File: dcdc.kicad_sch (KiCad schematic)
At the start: 198 parts, among them U11 SIC431AED-T1-GE3, U12 SIC431AED-T1-GE3, U13 SIC431AED-T1-GE3, U22 INA219AIDCNR, U50 INA219AIDCNR, U60 INA219AIDCNR, U65 SIC431AED-T1-GE3, U66 INA219AIDCNR, U69 TPS564247DRLR, U7 TPS564247DRLR, U75 SIC431AED-T1-GE3, U76 INA219AIDCNR, U8 SIC431AED-T1-GE3

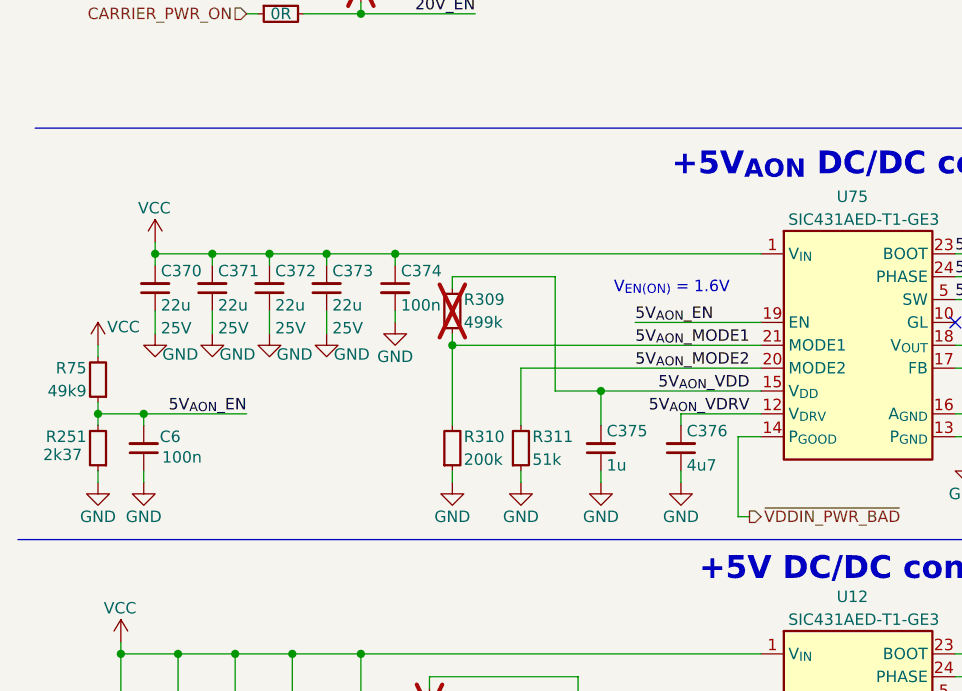
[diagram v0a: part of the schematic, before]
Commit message: Fix R251 symbol on schematic, improve readability of U75 EN voltage divider
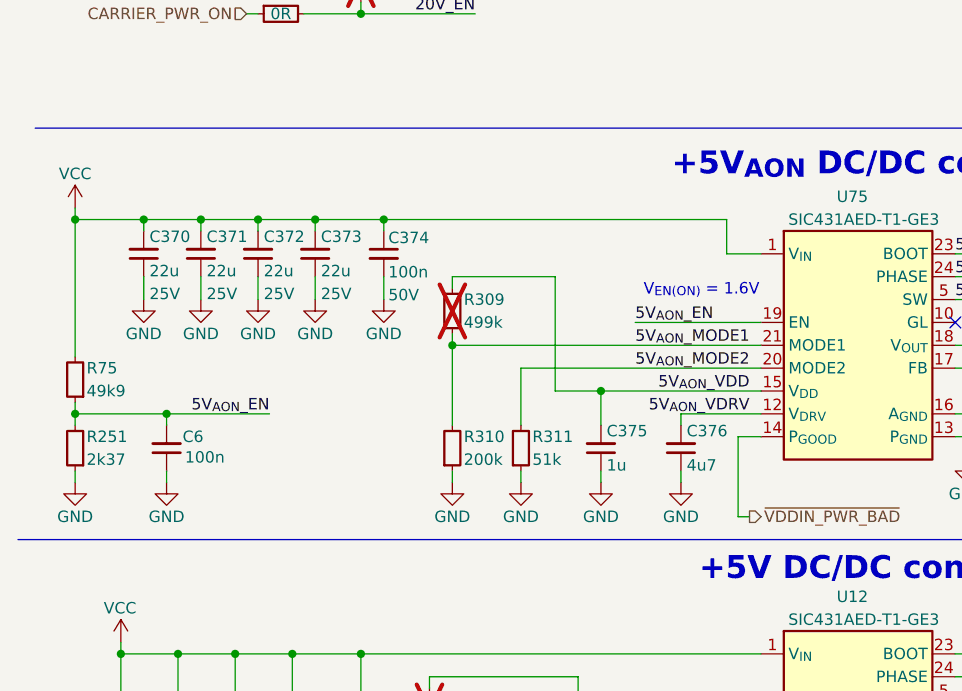
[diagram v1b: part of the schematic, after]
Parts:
- R251: value R_499k_0402 -> R_2k37_0402
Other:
- moved on the sheet: C370, C371, C372, C373, C374, C6, R251, R75

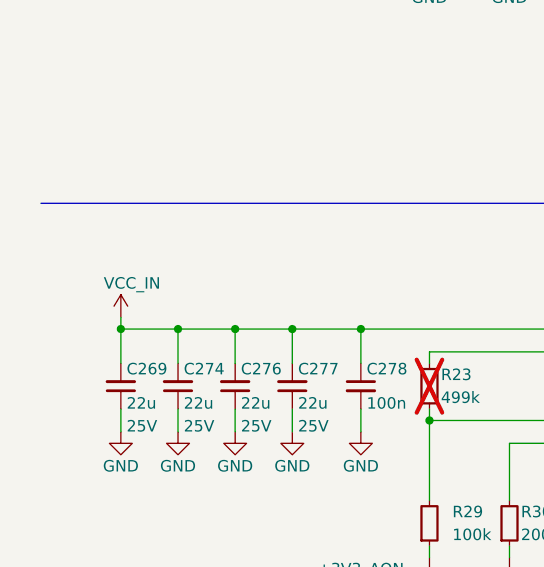
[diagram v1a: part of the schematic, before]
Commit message: Fix +20V converter now is power up from Vcc not Vcc_in
After this change +20V DC/DC converter is safe from reverse voltage
connected to board
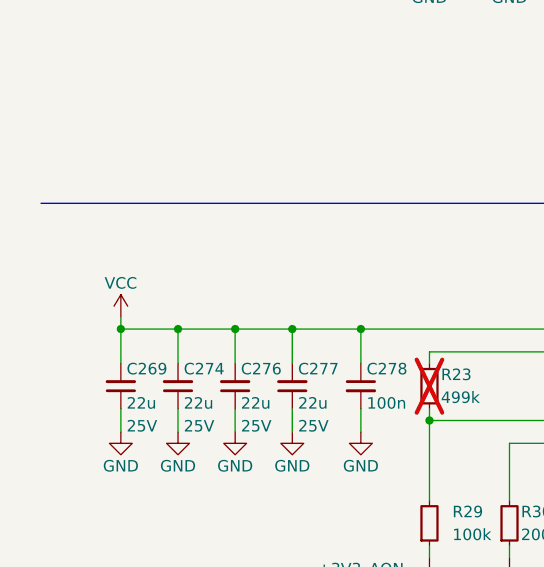
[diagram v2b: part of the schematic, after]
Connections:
- net VCC_IN is gone; now on net VCC: C269.2, C274.2, C276.2, C277.2, C278.1, U65.1 (V_{IN}), U65.2 (V_{IN}), U65.22 (V_{IN}), U65.26 (V_{IN})
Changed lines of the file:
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@@
 	(symbol
 		(lib_id "antmicropower:VCC")
-		(at 16.51 157.48 0)
+		(at 21.59 95.25 0)
 		(unit 1)
 		(exclude_from_sim no)
@@
 		(dnp no)
 		(property "Reference" "#PWR0663"
-			(at 16.51 161.29 0)
+			(at 21.59 99.06 0)
 			(effects
 				(font
@@
 		)
 		(property "Value" "VCC"
-			(at 16.51 153.67 0)
+			(at 21.59 91.44 0)
 			(effects
 				(font
@@
 		)
 		(property "Footprint" ""
-			(at 16.51 157.48 0)
+			(at 21.59 95.25 0)
 			(effects
 				(font
@@
 		)
 		(property "Datasheet" ""
-			(at 16.51 157.48 0)
+			(at 21.59 95.25 0)
 			(effects
 				(font
@@
 		)
 		(property "Description" ""
-			(at 16.51 157.48 0)
+			(at 21.59 95.25 0)
 			(effects
 				(font
@@
 	)
 	(symbol
-		(lib_id "antmicropower:VCC")
-		(at 21.59 95.25 0)
-		(unit 1)
-		(exclude_from_sim no)
-		(in_bom yes)
-		(on_board yes)
-		(dnp no)
-		(property "Reference" "#PWR0573"
-			(at 21.59 99.06 0)
-			(effects
-				(font
-					(size 1.27 1.27)
-				)
-				(justify left bottom)
-				(hide yes)
-			)
-		)
-		(property "Value" "VCC_IN"
-			(at 19.685 91.44 0)
-			(effects
-				(font
-					(size 1.27 1.27)
-				)
-				(justify left)
-			)
-		)
-		(property "Footprint" ""
-			(at 21.59 95.25 0)
-			(effects
-				(font
-					(size 1.27 1.27)
-				)
-				(hide yes)
-			)
-		)
-		(property "Datasheet" ""
-			(at 21.59 95.25 0)
-			(effects
-				(font
-					(size 1.27 1.27)
-				)
-				(hide yes)
-			)
-		)
-		(property "Description" ""
-			(at 21.59 95.25 0)
-			(effects
-				(font
-					(size 1.27 1.27)
-				)
-				(hide yes)
-			)
-		)
-		(pin "1"
-		)
-		(instances
-			(project "jetson-agx-thor-baseboard"
-				(path "/f569b0be-0afd-48b7-93ee-28582a4c645c/24bfa3d1-0a03-41a0-8beb-0ef00bfb4ba3"
-					(reference "#PWR0573")
-					(unit 1)
-				)
-			)
-		)
-	)
-	(symbol
 		(lib_id "antmicroCapacitorsmisc:C_22u_25V_0805")
 		(at 162.56 124.46 90)
@@
 					(unit 1)
 				)
+			)
+		)
+	)
+	(symbol
+		(lib_id "antmicropower:VCC")
+		(at 16.51 157.48 0)
+		(unit 1)
+		(exclude_from_sim no)
+		(in_bom yes)
+		(on_board yes)
+		(dnp no)
+		(property "Reference" "#PWR0491"
+			(at 16.51 161.29 0)
+			(effects
+				(font
+					(size 1.27 1.27)
+				)
+				(justify left bottom)
+				(hide yes)
+			)
+		)
+		(property "Value" "VCC"
+			(at 16.51 153.67 0)
+			(effects
+				(font
+					(size 1.27 1.27)
+				)
+			)
+		)
+		(property "Footprint" ""
+			(at 16.51 157.48 0)
+			(effects
+				(font
+					(size 1.27 1.27)
+				)
+				(hide yes)
+			)
+		)
+		(property "Datasheet" ""
+			(at 16.51 157.48 0)
+			(effects
+				(font
+					(size 1.27 1.27)
+				)
+				(hide yes)
+			)
+		)
+		(property "Description" ""
+			(at 16.51 157.48 0)
+			(effects
+				(font
+					(size 1.27 1.27)
+				)
+				(hide yes)
+			)
+		)
+		(pin "1"
+		)
+		(instances
+			(project "jetson-agx-thor-baseboard"
+				(path "/f569b0be-0afd-48b7-93ee-28582a4c645c/24bfa3d1-0a03-41a0-8beb-0ef00bfb4ba3"
+					(reference "#PWR0491")
+					(unit 1)
+				)
